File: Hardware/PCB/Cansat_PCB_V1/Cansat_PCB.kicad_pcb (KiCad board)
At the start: 2 copper layers, 25 x 25 mm, 86 parts, among them IC1 Alim STM Baro GPS IMU, IC2 Alim STM Baro GPS IMU, J1 Lecteur SD, J2 Connecteur Batterie, J3 Connecteur STLINK, J4 Connecteur Moteur, J4 Connecteur moteur, J5 Connecteur GPS, J6 Connecteur GPS, J7 Connecteur LoRa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

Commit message: routage non fini : ceci est un commit de transfert de fichier vers un autre PC
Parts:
- C21, C24, J4, L1, R19, R20, R21: moved to B.Cu
- moved R15 68.5 mm to (144.3, 106.4), turned to 180 degrees
- moved R17 67.2 mm to (150.6, 111.9), turned to 180 degrees
- moved C17 65.7 mm to (156.5, 110.5)
- moved R16 65.6 mm to (143.7, 104.8), turned to 90 degrees
- moved R18 64.4 mm to (150.6, 110.8)
- moved C18 62.6 mm to (142.1, 105.4), turned to 180 degrees
- moved C19 61.8 mm to (142.0, 106.5), turned to 180 degrees
- moved C9 60.6 mm to (152.7, 105.3), turned to 90 degrees
- moved C20 60.1 mm to (151.4, 109.7)
- moved R13 58.6 mm to (154.7, 111.3), turned to 90 degrees
- moved R10 56.1 mm to (160.2, 104.2), turned to 90 degrees
- moved C10 55.8 mm to (145.1, 100.4)
- moved R14 55.6 mm to (158.1, 111.2), turned to 90 degrees
- moved R7 55.1 mm to (149.7, 109.0), turned to 90 degrees
- moved R12 54.9 mm to (161.8, 107.3), turned to -90 degrees
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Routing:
- net +3.3V: track 0.00 -> 32.7 mm
- net IMU_INT: track 0.00 -> 22.8 mm, vias 0 -> 2
- net VDDIO: track 0.00 -> 19.9 mm
- net I2C1_SDA: track 0.00 -> 13.8 mm, vias 0 -> 2
- net BAROEXTI: track 0.00 -> 13.5 mm, vias 0 -> 2
- net SPI1_SCK_SD: track 0.00 -> 12.0 mm, vias 0 -> 2
- net SPI1_MISO_SD: track 0.00 -> 11.3 mm
- net Net-(U2-PF0): track 0.00 -> 8.37 mm
- net Net-(U1-INT): track 0.00 -> 8.18 mm, vias 0 -> 2
- net SDDETECT: track 0.00 -> 7.44 mm
- net SPI1_MOSI_SD: track 0.00 -> 7.09 mm
- net GND: track 0.00 -> 7.01 mm
- net SPI1_CS_SD: track 0.00 -> 6.30 mm
- net Net-(U2-PF1): track 0.00 -> 5.36 mm
- net Net-(U3-XOUT32): track 0.00 -> 5.34 mm
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- added copper zone on F.Cu, net GND
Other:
- board size 25 x 25 mm -> 25.8 x 25.8 mm

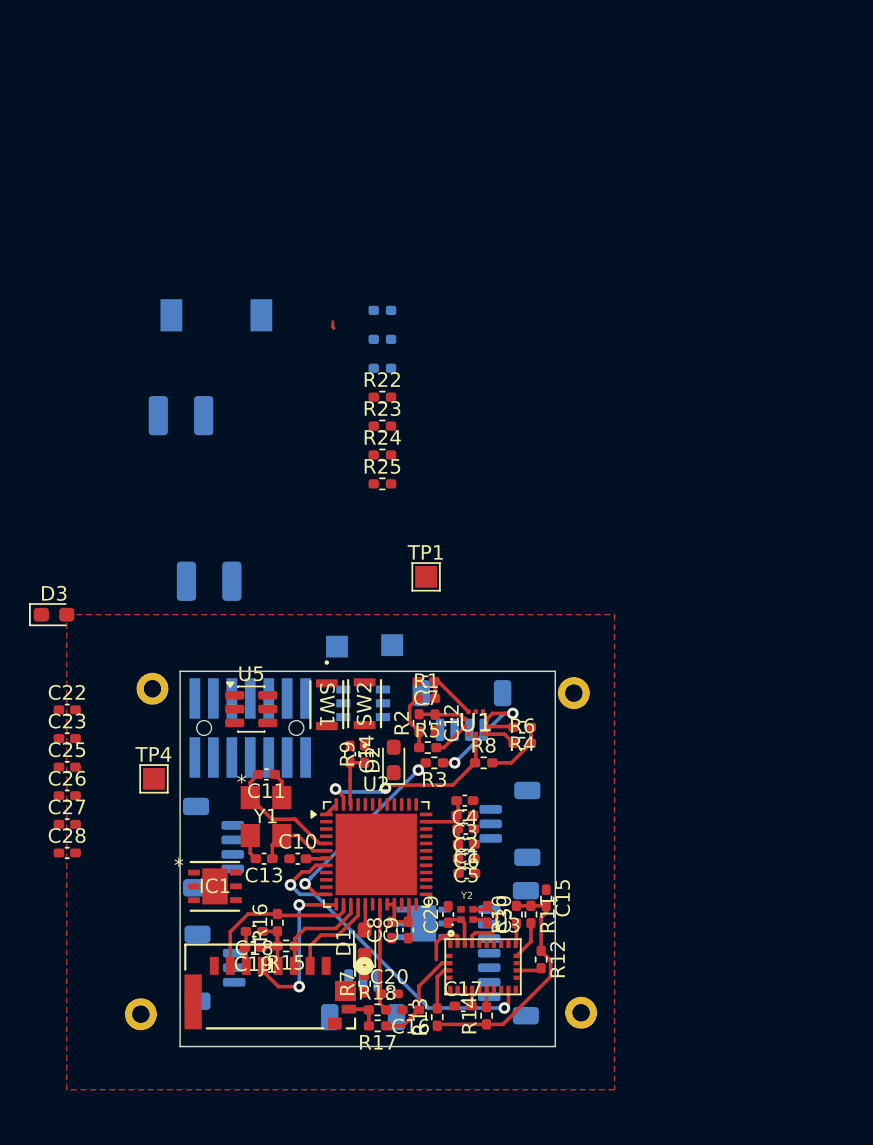
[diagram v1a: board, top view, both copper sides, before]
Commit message: nouvelles règles de routage Attention les pistes sont à l'ancienne taille : a corriger
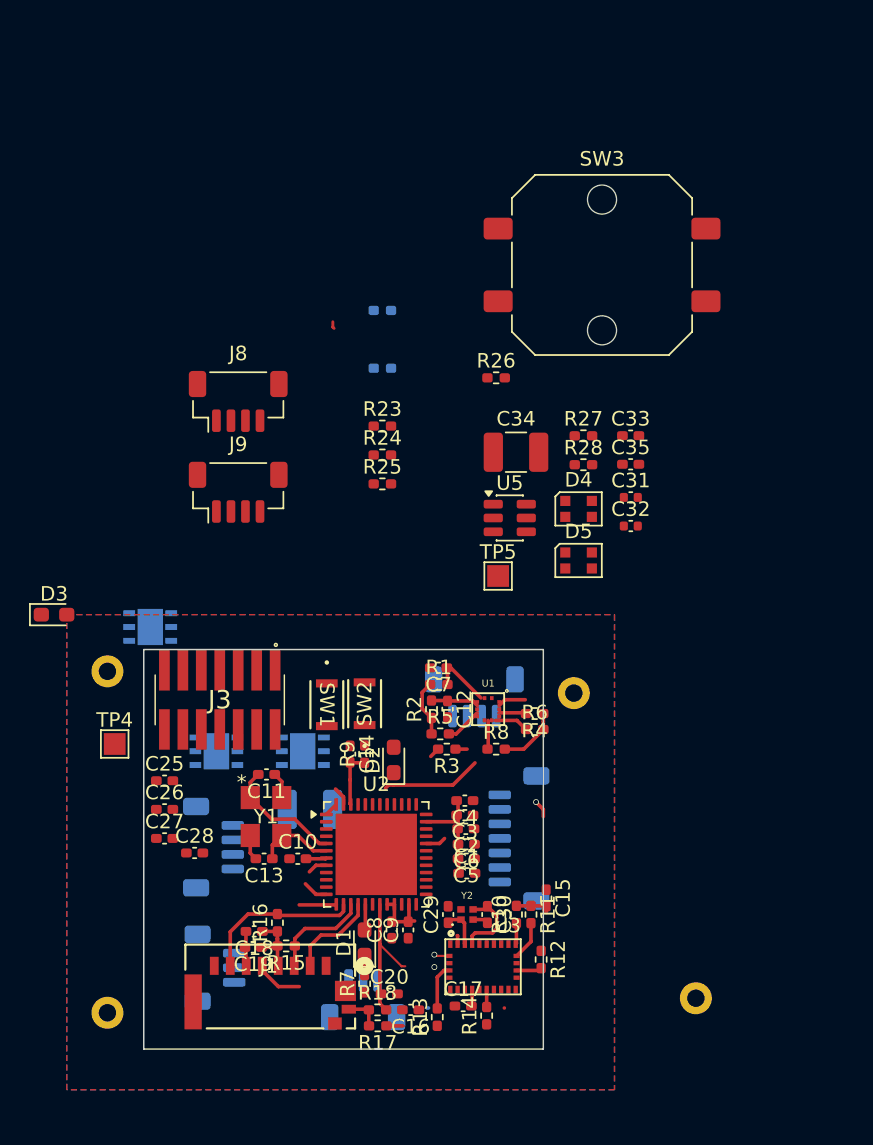
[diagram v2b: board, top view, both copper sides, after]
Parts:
- removed C21: 0.1u, Capacitor_SMD:C_1210_3225Metric_Pad1.33x2.70mm_HandSolder
- removed C22: 66u, Capacitor_SMD:C_0402_1005Metric_Pad0.74x0.62mm_HandSolder
- removed C23: 2.2u, Capacitor_SMD:C_0402_1005Metric_Pad0.74x0.62mm_HandSolder
- removed the J4 at (159.7, 98.0)
- removed R20: 53.6k, Resistor_SMD:R_0402_1005Metric_Pad0.72x0.64mm_HandSolder
- removed R22: 10.2k, Resistor_SMD:R_0402_1005Metric_Pad0.72x0.64mm_HandSolder
- removed TP1, TP2, TP3: TestPoint, TestPoint:TestPoint_Pad_1.5x1.5mm
- removed U4: Adaptateur USB, footprints:SOT23-6L_STM
- added C31: 100n, Capacitor_SMD:C_0402_1005Metric, F.Cu at (168.0, 75.5)
- added C32: 100n, Capacitor_SMD:C_0402_1005Metric, F.Cu at (168.0, 77.5)
- added C33: 2.2u, Capacitor_SMD:C_0402_1005Metric_Pad0.74x0.62mm_HandSolder, F.Cu at (168.0, 71.3)
- added C34: 0.1u, Capacitor_SMD:C_1210_3225Metric_Pad1.33x2.70mm_HandSolder, F.Cu at (160.1, 72.4)
- added C35: 66u, Capacitor_SMD:C_0402_1005Metric_Pad0.74x0.62mm_HandSolder, F.Cu at (168.0, 73.2)
- added D4: WS2812B-2020, LED_SMD:LED_WS2812B-2020_PLCC4_2.0x2.0mm, F.Cu at (164.4, 76.3)
- added D5: WS2812B-2020, LED_SMD:LED_WS2812B-2020_PLCC4_2.0x2.0mm, F.Cu at (164.4, 79.9)
- added J8: connecteurb IHM, Connector_JST:JST_SH_BM04B-SRSS-TB_1x04-1MP_P1.00mm_Vertical, F.Cu at (141.0, 68.9)
- added J9: Connecteur IHM, Connector_JST:JST_SH_BM04B-SRSS-TB_1x04-1MP_P1.00mm_Vertical, F.Cu at (141.0, 75.2)
- added R26: 330, Resistor_SMD:R_0402_1005Metric_Pad0.72x0.64mm_HandSolder, F.Cu at (158.8, 67.3)
- added R27: 10.2k, Resistor_SMD:R_0402_1005Metric_Pad0.72x0.64mm_HandSolder, F.Cu at (164.8, 71.3)
- added R28: 53.6k, Resistor_SMD:R_0402_1005Metric_Pad0.72x0.64mm_HandSolder, F.Cu at (164.8, 73.3)
- added SW3: SW_Push, Button_Switch_SMD:SW_Push_1P1T_NO_CK_PTS125Sx43PSMTR, F.Cu at (166.0, 59.5)
- added TP5: TestPoint, TestPoint:TestPoint_Pad_1.5x1.5mm, F.Cu at (158.9, 80.9)
- H1, H2, H3, H4: footprint customhole:mountinghole1.2mm -> footprints:mountinghole1.2mm
- IC1: moved to B.Cu
- J3: footprint footprints:SAMTEC_FTSH-107-01-L-DV-K-A -> footprints:FTSH-107-XX-YYY-DV-K; moved to F.Cu
- J4: value Connecteur moteur -> Connecteur Moteur
- L1: footprint footprints:IND_WE-PD-SMT_7332_WRE -> footprints:DFN6_3X3_STM
- U1: footprint bmp581:BMP581 -> footprints:BMP581
- U5: value Alim 5V -> LMR51625
- moved L1 30.0 mm to (139.5, 93.0)
- moved U5 22.1 mm to (159.7, 76.9)
- moved IC1 18.4 mm to (134.9, 84.5), turned to 180 degrees
- moved C24 17.2 mm to (145.9, 97.0)
- moved IC2 14.5 mm to (145.4, 93.0)
- moved C28 8.77 mm to (138.0, 100.0)
- moved H2 7.96 mm to (172.5, 110.0)
- moved J7 7.93 mm to (160.3, 99.0)
- moved C27 6.77 mm to (135.9, 99.0)
- moved C25 6.77 mm to (135.9, 95.0)
- moved C26 6.77 mm to (135.9, 97.0)
- moved TP4 3.61 mm to (132.5, 92.5)
- moved H3 3.32 mm to (132.0, 87.5)
- moved J3 2.86 mm to (139.7, 89.5)
- moved H4 2.30 mm to (132.0, 111.0)
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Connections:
- C15 pad 2: VDDIO -> +3.3V
- J4 pad 1: GND -> TIM3_CHI_PWM4
- J4 pad 3: TIM3_CHI_PWM4 -> GND
- R10 pad 2: VDDIO -> +3.3V
- R11 pad 1: VDDIO -> +3.3V
- R12 pad 1: VDDIO -> +3.3V
- R13 pad 1: VDDIO -> +3.3V
- R14 pad 1: VDDIO -> +3.3V
- U2 pad 11: unconnected-(U2-PA3-Pad11) -> EXTI3
- U2 pad 22: unconnected-(U2-PB10-Pad22) -> Net-(U2-PB10)
- U2 pad 33: D- -> unconnected-(U2-PA11-Pad33)
- U2 pad 34: D+ -> unconnected-(U2-PA12-Pad34)
- U3 pad 28: VDDIO -> +3.3V
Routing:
- net IMU_INT: track 22.8 -> 1.35 mm, vias 2 -> 0
- net VDDIO: track 19.9 -> 0.00 mm
- net BAROEXTI: track 13.5 -> 2.45 mm, vias 2 -> 0
- net Net-(U1-INT): track 8.18 -> 0.80 mm, vias 2 -> 0
- net SPI1_SCK_SD: track 12.0 -> 6.34 mm, vias 2 -> 0
- net (no net): track 0.00 -> 4.46 mm, vias 0 -> 2
- net USART1_STLINK_RX: track 0.00 -> 4.12 mm
- net I2C1_SDA: track 13.8 -> 10.2 mm, vias 2 -> 0
- net SDDETECT: track 7.44 -> 9.81 mm
- net +3.3V: track 32.7 -> 30.5 mm
- net Net-(U1-VDD): track 4.38 -> 6.35 mm
- net GND: track 7.01 -> 8.08 mm, vias 0 -> 1
- added copper zone on B.Cu, net GND
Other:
- board size 25.8 x 25.8 mm -> 27.5 x 27.5 mm
- copper layers 2 -> 6
- board text added: "1-Signal 2-GND 3-Signal 4-PWR 5-GND 6-Signal"

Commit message: Organisation des 6 couches + Placement des différents composants avant routage
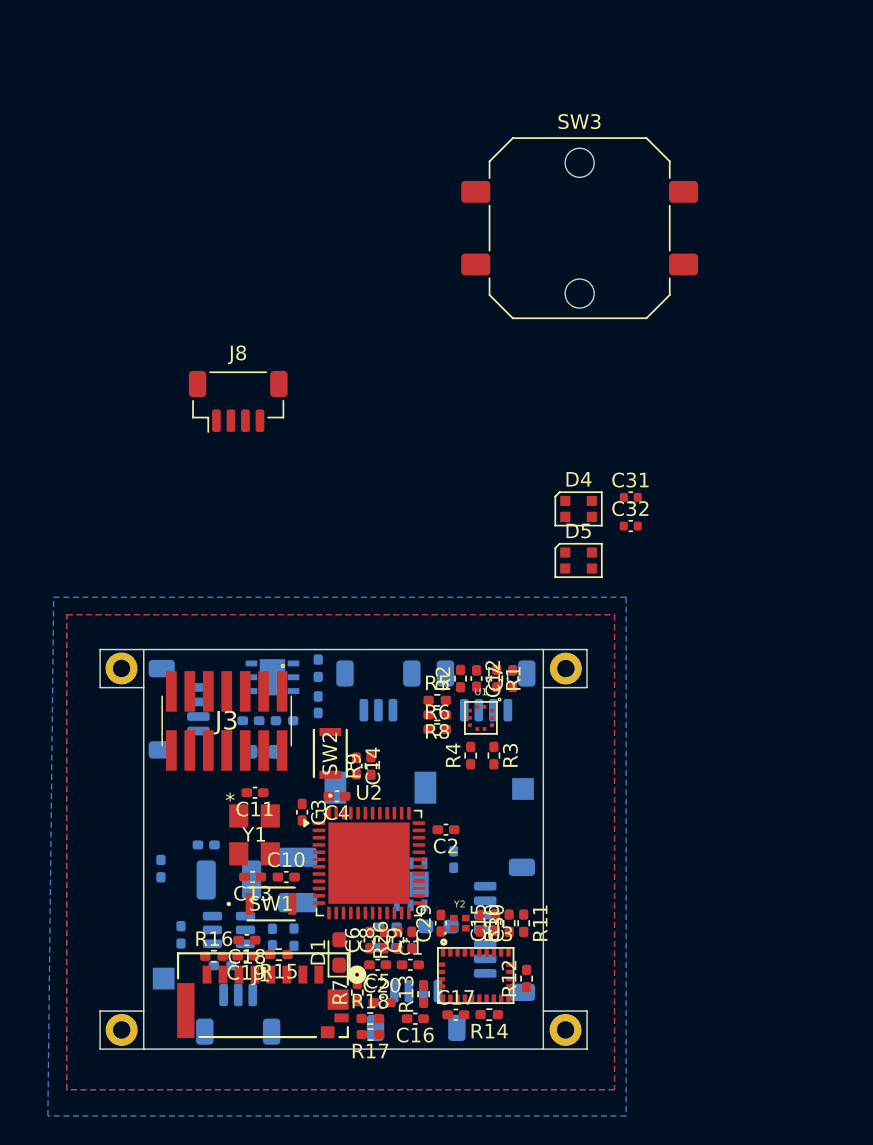
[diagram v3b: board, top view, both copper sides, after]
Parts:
- C25, C26, C27, C28, C33, C34, C35, D2, D3, J9, R23, R24, R25, R27, R28, TP4, TP5, U5: moved to B.Cu
- L1: footprint footprints:DFN6_3X3_STM -> footprints:IND_WE-PD-SMT_7332_WRE
- moved R19 45.2 mm to (137.1, 105.6), turned to -90 degrees
- moved R27 44.1 mm to (139.9, 107.8)
- moved C33 42.4 mm to (143.4, 105.8), turned to 90 degrees
- moved R28 40.2 mm to (135.7, 101.1), turned to 90 degrees
- moved R21 39.6 mm to (144.8, 105.8), turned to -90 degrees
- moved R26 39.3 mm to (152.0, 106.0), turned to 90 degrees
- moved C35 39.2 mm to (138.8, 99.5), turned to 180 degrees
- moved J9 37.7 mm to (153.2, 110.8)
- moved C34 35.5 mm to (140.4, 101.9)
- moved R23 34.5 mm to (151.3, 105.1)
- moved U5 34.3 mm to (140.4, 105.3), turned to 180 degrees
- moved IC1 25.2 mm to (152.9, 102.2), turned to -90 degrees
- moved J4 22.1 mm to (150.7, 88.8), turned to 180 degrees
- moved J5 21.6 mm to (158.1, 88.8), turned to 180 degrees
- moved J6 20.3 mm to (136.9, 90.1), turned to -90 degrees
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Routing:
- net +3.3V: track 30.5 -> 0.00 mm
- net SPI1_MISO_SD: track 11.3 -> 0.00 mm
- net I2C1_SDA: track 10.2 -> 0.00 mm
- net SDDETECT: track 9.81 -> 0.00 mm
- net Net-(U2-PF0): track 8.37 -> 0.00 mm
- net GND: track 8.08 -> 0.00 mm, vias 1 -> 0
- net SPI1_MOSI_SD: track 7.09 -> 0.00 mm
- net Net-(U1-VDD): track 6.35 -> 0.00 mm
- net SPI1_SCK_SD: track 6.34 -> 0.00 mm
- net SPI1_CS_SD: track 6.30 -> 0.00 mm
- net Net-(U2-PF1): track 5.36 -> 0.00 mm
- net Net-(U3-XOUT32): track 5.34 -> 0.00 mm
- net (no net): track 4.46 -> 0.05 mm, vias 2 -> 0
- net USART1_STLINK_RX: track 4.12 -> 0.00 mm
- net Net-(U2-PB8): track 3.89 -> 0.00 mm
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- added copper zone on In1.Cu, net GND
- added copper zone on In2.Cu, net GND
- added copper zone on In3.Cu, net GND
- added copper zone on In4.Cu, net GND
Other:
- board size 27.5 x 27.5 mm -> 33.5 x 27.5 mm

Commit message: Début du routage
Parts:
- moved C3 11.9 mm to (153.3, 106.1), turned to 180 degrees
- moved R19 8.29 mm to (144.9, 108.3)
- moved SW1 4.87 mm to (138.4, 103.2)
- moved C9 4.77 mm to (148.2, 106.8), turned to 0 degrees
- moved R28 4.66 mm to (137.2, 105.5)
- moved R7 4.16 mm to (145.9, 107.0), turned to 180 degrees
- moved C11 3.65 mm to (144.9, 98.2), turned to -90 degrees
- moved D1 3.11 mm to (145.2, 105.5), turned to 0 degrees
- moved C8 2.80 mm to (148.2, 105.8), turned to 0 degrees
- moved C16 2.58 mm to (152.8, 108.8), turned to -90 degrees
- moved C25 2.50 mm to (153.2, 105.0)
- moved D2 2.34 mm to (152.8, 106.3)
- moved R23 2.24 mm to (150.4, 107.2), turned to 90 degrees
- moved C10 1.66 mm to (144.1, 103.3), turned to 90 degrees
- moved TP5 1.60 mm to (159.0, 95.5)
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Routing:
- net GND: vias 0 -> 5
- net +3.3V: vias 0 -> 4
- added copper zone on F.Cu, net +3.3V
- added copper zone on In3.Cu, net +3.3V
- removed copper zone on In3.Cu, net GND
